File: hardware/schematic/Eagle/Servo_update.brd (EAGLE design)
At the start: 100 x 80 mm, 40 parts

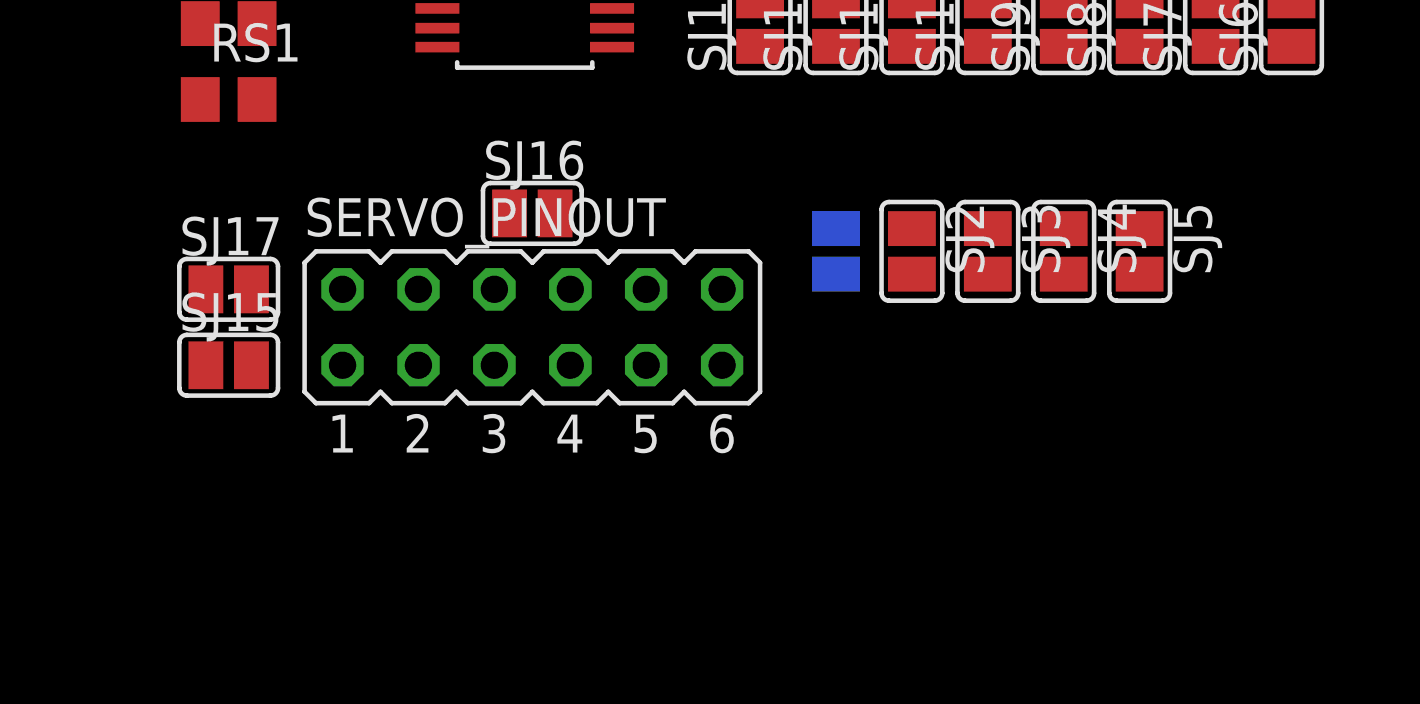
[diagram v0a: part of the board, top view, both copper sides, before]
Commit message: Updated Schematic with Dr.Week's Advice
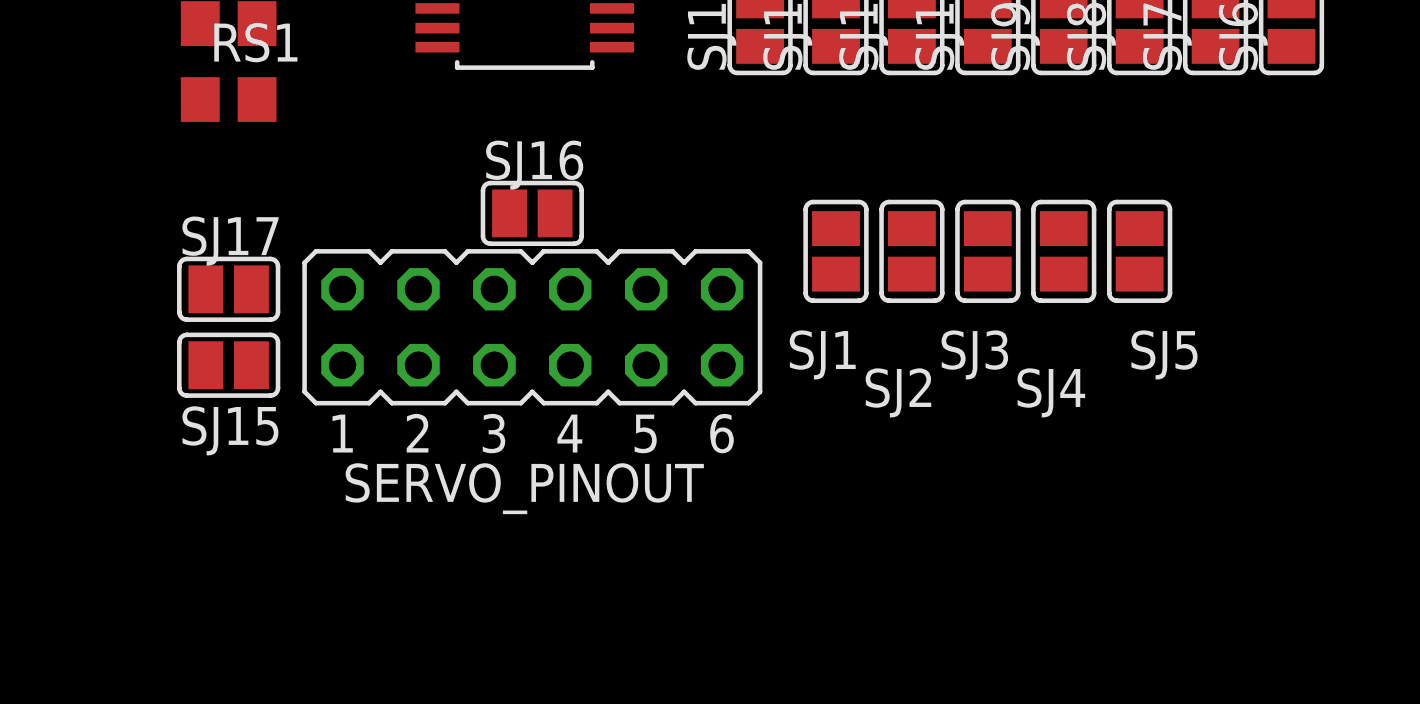
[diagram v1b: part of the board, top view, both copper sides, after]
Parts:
- flipped SJ1 to the top
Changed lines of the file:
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@@
 <drawing>
 <settings>
-<setting alwaysvectorfont="no"/>
+<setting alwaysvectorfont="yes"/>
 <setting verticaltext="up"/>
 </settings>
@@
 </element>
 <element name="SERVO_PINOUT" library="jumper" library_urn="urn:adsk.eagle:library:252" package="JP6Q" package3d_urn="urn:adsk.eagle:package:15457/1" value="" x="36.83" y="17.78" smashed="yes">
-<attribute name="NAME" x="29.21" y="20.828" size="1.27" layer="25" ratio="10"/>
+<attribute name="NAME" x="30.48" y="11.938" size="1.27" layer="25" ratio="10"/>
 <attribute name="POPULARITY" value="3" x="58.42" y="-52.07" size="1.778" layer="27" display="off"/>
 <attribute name="VALUE" x="29.21" y="12.192" size="1.27" layer="27" ratio="10"/>
@@
 <attribute name="VALUE" x="45.72" y="34.29" size="1.27" layer="27"/>
 </element>
-<element name="SJ1" library="jumper" library_urn="urn:adsk.eagle:library:252" package="SJ" package3d_urn="urn:adsk.eagle:package:15471/1" value="" x="46.99" y="20.32" smashed="yes" rot="MR270">
-<attribute name="NAME" x="45.847" y="21.971" size="1.27" layer="26" ratio="10" rot="MR270"/>
-<attribute name="POPULARITY" value="33" x="46.99" y="20.32" size="1.778" layer="28" rot="MR270" display="off"/>
-<attribute name="VALUE" x="46.99" y="19.9199" size="0.02" layer="28" rot="MR270"/>
+<element name="SJ1" library="jumper" library_urn="urn:adsk.eagle:library:252" package="SJ" package3d_urn="urn:adsk.eagle:package:15471/1" value="" x="46.99" y="20.32" smashed="yes" rot="R270">
+<attribute name="NAME" x="45.339" y="16.383" size="1.27" layer="25" ratio="10"/>
+<attribute name="POPULARITY" value="33" x="46.99" y="20.32" size="1.778" layer="27" rot="R270" display="off"/>
+<attribute name="VALUE" x="46.99" y="19.9199" size="0.02" layer="27" rot="R270"/>
 </element>
 <element name="SJ2" library="jumper" library_urn="urn:adsk.eagle:library:252" package="SJ" package3d_urn="urn:adsk.eagle:package:15471/1" value="" x="49.53" y="20.32" smashed="yes" rot="R270">
-<attribute name="NAME" x="50.673" y="21.971" size="1.27" layer="25" ratio="10" rot="R270"/>
+<attribute name="NAME" x="47.879" y="15.113" size="1.27" layer="25" ratio="10"/>
 <attribute name="POPULARITY" value="33" x="49.53" y="20.32" size="1.778" layer="27" rot="R270" display="off"/>
 <attribute name="VALUE" x="49.53" y="19.9199" size="0.02" layer="27" rot="R270"/>
 </element>
 <element name="SJ3" library="jumper" library_urn="urn:adsk.eagle:library:252" package="SJ" package3d_urn="urn:adsk.eagle:package:15471/1" value="" x="52.07" y="20.32" smashed="yes" rot="R270">
-<attribute name="NAME" x="53.213" y="21.971" size="1.27" layer="25" ratio="10" rot="R270"/>
+<attribute name="NAME" x="50.419" y="16.383" size="1.27" layer="25" ratio="10"/>
 <attribute name="POPULARITY" value="33" x="52.07" y="20.32" size="1.778" layer="27" rot="R270" display="off"/>
 <attribute name="VALUE" x="52.07" y="19.9199" size="0.02" layer="27" rot="R270"/>
 </element>
 <element name="SJ4" library="jumper" library_urn="urn:adsk.eagle:library:252" package="SJ" package3d_urn="urn:adsk.eagle:package:15471/1" value="" x="54.61" y="20.32" smashed="yes" rot="R270">
-<attribute name="NAME" x="55.753" y="21.971" size="1.27" layer="25" ratio="10" rot="R270"/>
+<attribute name="NAME" x="52.959" y="15.113" size="1.27" layer="25" ratio="10"/>
 <attribute name="POPULARITY" value="33" x="54.61" y="20.32" size="1.778" layer="27" rot="R270" display="off"/>
 <attribute name="VALUE" x="54.61" y="19.9199" size="0.02" layer="27" rot="R270"/>
 </element>
 <element name="SJ5" library="jumper" library_urn="urn:adsk.eagle:library:252" package="SJ" package3d_urn="urn:adsk.eagle:package:15471/1" value="" x="57.15" y="20.32" smashed="yes" rot="R270">
-<attribute name="NAME" x="58.293" y="21.971" size="1.27" layer="25" ratio="10" rot="R270"/>
+<attribute name="NAME" x="56.769" y="16.383" size="1.27" layer="25" ratio="10"/>
 <attribute name="POPULARITY" value="33" x="57.15" y="20.32" size="1.778" layer="27" rot="R270" display="off"/>
 <attribute name="VALUE" x="57.15" y="19.9199" size="0.02" layer="27" rot="R270"/>
@@
 </element>
 <element name="SJ15" library="jumper" library_urn="urn:adsk.eagle:library:252" package="SJ" package3d_urn="urn:adsk.eagle:package:15471/1" value="" x="26.67" y="16.51" smashed="yes">
-<attribute name="NAME" x="25.019" y="17.653" size="1.27" layer="25" ratio="10"/>
+<attribute name="NAME" x="25.019" y="13.843" size="1.27" layer="25" ratio="10"/>
 <attribute name="POPULARITY" value="33" x="26.67" y="16.51" size="1.778" layer="27" display="off"/>
 <attribute name="VALUE" x="27.0701" y="16.51" size="0.02" layer="27"/>
@@
 <wire x1="48.26" y1="34.29" x2="50.8" y2="39.895" width="0" layer="19" extent="1-1"/>
 <wire x1="48.26" y1="31.75" x2="48.26" y2="34.29" width="0" layer="19" extent="1-1"/>
+<wire x1="46.99" y1="28.702" x2="46.67" y2="31.75" width="0" layer="19" extent="1-1"/>
+<wire x1="49.53" y1="28.702" x2="46.99" y2="28.702" width="0" layer="19" extent="1-1"/>
+<wire x1="52.07" y1="28.702" x2="49.53" y2="28.702" width="0" layer="19" extent="1-1"/>
+<wire x1="54.61" y1="28.702" x2="52.07" y2="28.702" width="0" layer="19" extent="1-1"/>
+<wire x1="57.15" y1="28.702" x2="54.61" y2="28.702" width="0" layer="19" extent="1-1"/>
+<wire x1="59.69" y1="28.702" x2="57.15" y2="28.702" width="0" layer="19" extent="1-1"/>
+<wire x1="62.23" y1="28.702" x2="59.69" y2="28.702" width="0" layer="19" extent="1-1"/>
+<wire x1="44.45" y1="28.702" x2="46.99" y2="28.702" width="0" layer="19" extent="1-1"/>
 <wire x1="44.45" y1="36.83" x2="46.67" y2="34.29" width="0" layer="19" extent="1-1"/>
 <wire x1="42.86" y1="36.83" x2="44.45" y2="36.83" width="0" layer="19" extent="1-1"/>
-<wire x1="43.18" y1="16.51" x2="46.67" y2="31.75" width="0" layer="19" extent="1-1"/>
 <wire x1="39.497" y1="33.655" x2="42.86" y2="36.83" width="0" layer="19" extent="1-1"/>
-<wire x1="35.56" y1="16.51" x2="48.26" y2="31.75" width="0" layer="19" extent="1-1"/>
-<wire x1="35.56" y1="19.05" x2="35.56" y2="16.51" width="0" layer="19" extent="1-1"/>
 <wire x1="33.655" y1="27.1526" x2="39.497" y2="33.655" width="0" layer="19" extent="1-1"/>
 <wire x1="25.72" y1="27.94" x2="33.655" y2="27.1526" width="0" layer="19" extent="1-1"/>
@@
 <wire x1="25.72" y1="38.1" x2="25.72" y2="35.56" width="0" layer="19" extent="1-1"/>
 <wire x1="25.72" y1="25.4" x2="25.72" y2="27.94" width="0" layer="19" extent="1-1"/>
-<wire x1="46.99" y1="19.558" x2="25.72" y2="25.4" width="0" layer="19" extent="1-1"/>
+<wire x1="35.56" y1="19.05" x2="33.655" y2="27.1526" width="0" layer="19" extent="1-1"/>
+<wire x1="35.56" y1="16.51" x2="35.56" y2="19.05" width="0" layer="19" extent="1-1"/>
+<wire x1="43.18" y1="16.51" x2="35.56" y2="16.51" width="0" layer="19" extent="1-1"/>
+<wire x1="46.99" y1="19.558" x2="43.18" y2="16.51" width="0" layer="19" extent="1-1"/>
 <wire x1="49.53" y1="19.558" x2="46.99" y2="19.558" width="0" layer="19" extent="1-1"/>
 <wire x1="52.07" y1="19.558" x2="49.53" y2="19.558" width="0" layer="19" extent="1-1"/>
 <wire x1="54.61" y1="19.558" x2="52.07" y2="19.558" width="0" layer="19" extent="1-1"/>
 <wire x1="57.15" y1="19.558" x2="54.61" y2="19.558" width="0" layer="19" extent="1-1"/>
-<wire x1="62.23" y1="28.702" x2="57.15" y2="19.558" width="0" layer="19" extent="1-1"/>
-<wire x1="62.23" y1="28.702" x2="59.69" y2="28.702" width="0" layer="19" extent="1-1"/>
-<wire x1="57.15" y1="28.702" x2="59.69" y2="28.702" width="0" layer="19" extent="1-1"/>
-<wire x1="54.61" y1="28.702" x2="57.15" y2="28.702" width="0" layer="19" extent="1-1"/>
-<wire x1="52.07" y1="28.702" x2="54.61" y2="28.702" width="0" layer="19" extent="1-1"/>
-<wire x1="49.53" y1="28.702" x2="52.07" y2="28.702" width="0" layer="19" extent="1-1"/>
-<wire x1="46.99" y1="28.702" x2="49.53" y2="28.702" width="0" layer="19" extent="1-1"/>
-<wire x1="44.45" y1="28.702" x2="46.99" y2="28.702" width="0" layer="19" extent="1-1"/>
 </signal>
 <signal name="N$1">
 <contactref element="SERVO_CONTROLLER" pad="9"/>
 <contactref element="SJ1" pad="1"/>
-<wire x1="46.99" y1="21.082" x2="33.655" y2="30.4038" width="0" layer="19" extent="1-1"/>
+<wire x1="33.655" y1="30.4038" x2="46.99" y2="21.082" width="0" layer="19" extent="1-1"/>
 </signal>
 <signal name="N$2">
